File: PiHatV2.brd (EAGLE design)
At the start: 65.8 x 56.4 mm, 29 parts, among them U1 RASPBERRY_PI_3_MODEL_B+, X2 SCREENBREAKOUT_SCREENBREAKOUT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

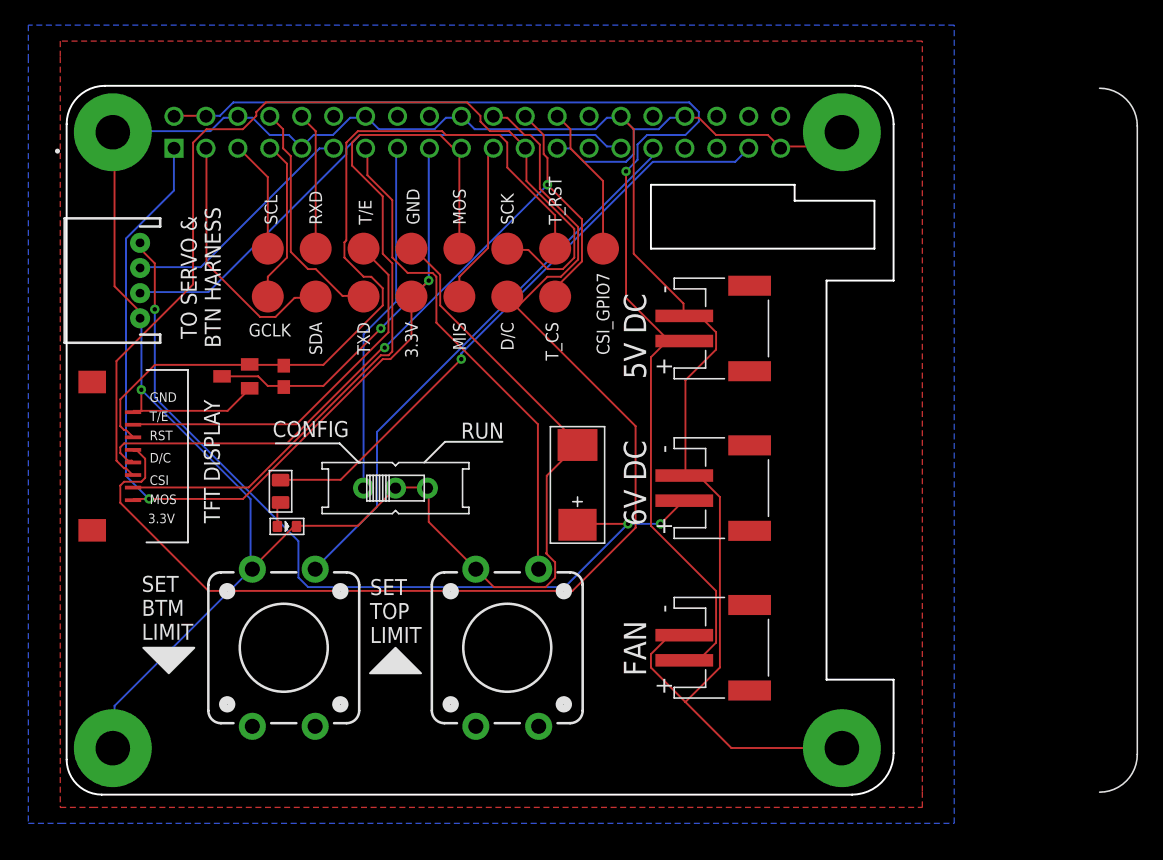
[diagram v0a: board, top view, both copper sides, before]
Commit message: support for a limit switch button for cont servo
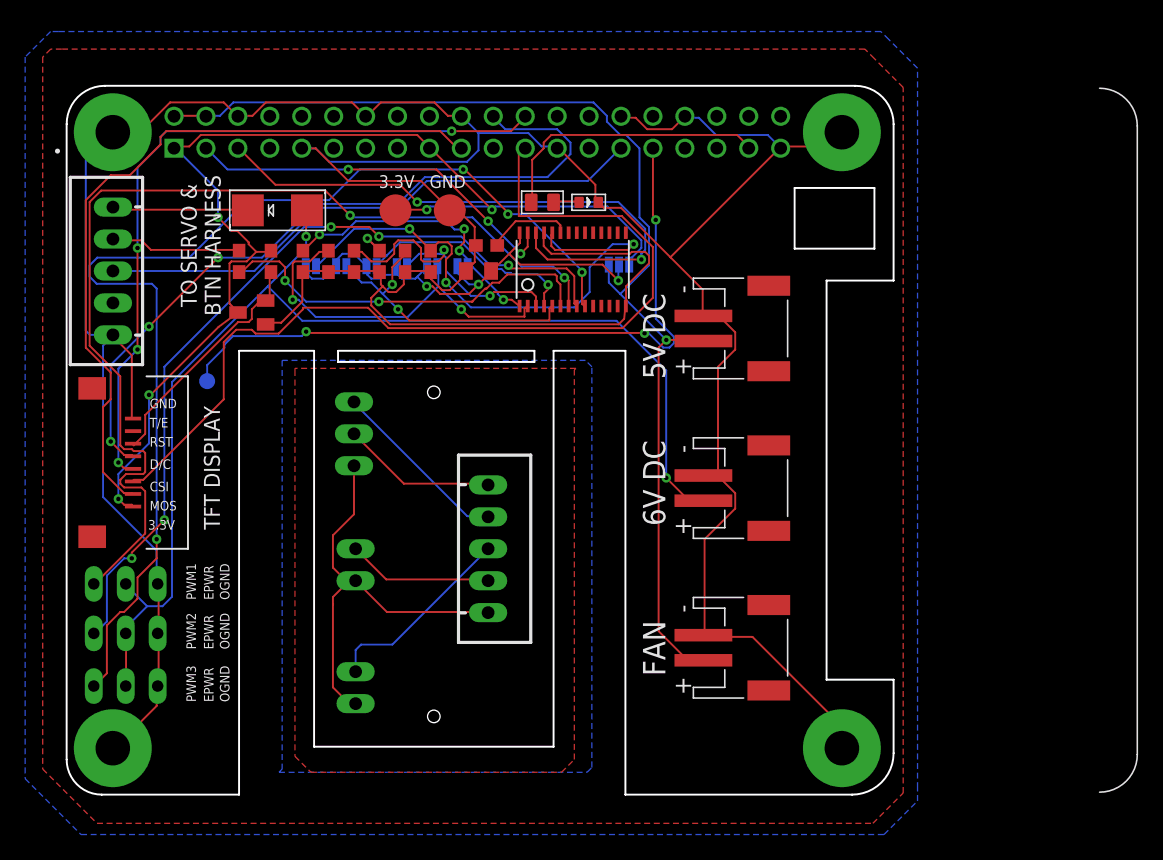
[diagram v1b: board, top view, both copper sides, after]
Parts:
- removed C1: 470uf, Seeed-Capacitor:AVX-D
- removed S1: (no value), adafruit:EG1218
- removed S2, S3: SPARKFUN-SWITCHES_MOMENTARY-SWITCH-SPST-PTH-12MM, ARDUINO_3V_TTL_INTERFACE_2_PI:SPARKFUN-SWITCHES_TACTILE_SWITCH_PTH_12MM
- removed SERVO_BTN_HARNESS: (no value), SparkFun-Connectors:JST-4-PTH
- removed TP1, TP10, TP11, TP12, TP13, TP14, TP15, TP2, TP3, TP4, TP5, TP6, TP9: TPB2,54, testpad:B2,54
- added C2: 10uF, adafruit:C0805K
- added D1: (no value), adafruit:SMADIODE
- added IO_LEVEL: JUMPER-SMT_3_NO_NO-SILK, SparkFun-Jumpers:SMT-JUMPER_3_NO_NO-SILK
- added JP1, JP2, JP3: (no value), FeatherWing:LED-BADGE_SCHEMATIC_JUMPER_JP2
- added JP4, JP5, JP6, JP7, JP8, JP9: JUMPER-SMT_2_NO_NO-SILK, SparkFun-Jumpers:SMT-JUMPER_2_NO_NO-SILK
- added LIM_BTN: TESTPAD_TPSQB1,27, ARDUINO_3V_TTL_INTERFACE_2_PI:TESTPAD_B1,27
- added R10, R2, R5, R6, R7, R8, R9: 10k, PiHat:ARDUINO_3V_TTL_INTERFACE_2_PI_SPARKFUN-RESISTORS_0603:1
- added R4: 220, PiHat:ARDUINO_3V_TTL_INTERFACE_2_PI_SPARKFUN-RESISTORS_0603:1
- added U2: (no value), adafruit:TSSOP28
- added X1, X3: JST-XH-05-PIN-LONG-PAD, Rembrandt Electronics - JST XH Connectors v1-0:JST-XH-05-PACKAGE-LONG-PAD
- added X4: JST-XH-03-PIN-LONG-PAD, Rembrandt Electronics - JST XH Connectors v1-0:JST-XH-03-PACKAGE-LONG-PAD
- added X5, X6: JST-XH-02-PIN-LONG-PAD, Rembrandt Electronics - JST XH Connectors v1-0:JST-XH-02-PACKAGE-LONG-PAD
- moved D2 35.2 mm to (44.6, 25.3)
- moved R3 31.0 mm to (40.9, 25.3), turned to 90 degrees
- moved R1 9.20 mm to (19.3, 20.6), turned to 270 degrees
- moved TP7 6.97 mm to (29.2, 24.6)
- moved APX803 5.24 mm to (17.8, 16.5)
- moved TP8 4.31 mm to (33.5, 24.6)
- moved 5V_IO 1.52 mm to (57.4, 15.2)
- moved FAN 1.52 mm to (57.4, -10.2)
- moved SERVO_PWR 1.52 mm to (57.4, 2.54)
- moved X2 0.51 mm to (5.08, 4.57)
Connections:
- removed net CONFIG: S1.O, U1.15
- removed net DOWN: S3.1, U1.31
- removed net GPCLK0: TP6.TP, U1.7
- removed net RX: TP3.TP, U1.10
- removed net TX: TP2.TP, U1.8
- removed net UP: S2.1, U1.13
- new net A0: JP4.1, R5.2, U2.1
- new net A1: JP5.1, R6.2, U2.2
- new net A2: JP6.1, R7.2, U2.3
- new net A3: JP7.1, R8.2, U2.4
- new net A4: JP8.1, R9.2, U2.5
- new net A5: JP9.1, R10.2, U2.24
- new net BB_BTN: X3.3, X6.2
- new net BB_GND: X3.5, X4.1, X5.1, X6.1
- new net BB_LIM_BTN: X3.4, X5.2
- new net BB_SERVO: X3.2, X4.3
- new net BB_SER_PWR: X3.1, X4.2
- new net LIM_BTN: LIM_BTN.TP, U1.31, X1.2
- new net N$5: R4.1, U2.6
- new net N$6: D1.C, X1.5
- new net OE: R2.2, U2.23
- new net PWM1: JP1.3, U2.7
- new net PWM2: JP2.3, U2.8
- new net PWM3: JP3.3, U2.9
- new net VDDIO: C2.1, IO_LEVEL.2, JP4.2, JP5.2, JP6.2, JP7.2, JP8.2, JP9.2, U2.28
- net 3.3V: now also IO_LEVEL.3
- net 5V: now also IO_LEVEL.1
- net BTN: now also X1.3; no longer SERVO_BTN_HARNESS.2
- net CS1: no longer TP15.TP
- net D/C: no longer TP12.TP
- net GND: now also C2.2, JP1.1, JP2.1, JP3.1, R10.1, R2.1, R5.1, R6.1, R7.1, R8.1, R9.1, U2.14, U2.25, X1.1; no longer C1.-, S1.P, S1.S, S2.3, S3.3, SERVO_BTN_HARNESS.1
- net MISO: no longer TP10.TP
- net MOSI: no longer TP9.TP
- net SCK: no longer TP11.TP
- net SCL: now also U2.26; no longer TP5.TP
- net SDA: now also U2.27; no longer TP4.TP
- net SERVO: now also R4.2, X1.4; no longer SERVO_BTN_HARNESS.3, U1.11
- net SER_PWR: now also D1.A, JP1.2, JP2.2, JP3.2; no longer C1.+, SERVO_BTN_HARNESS.4
- net TE: no longer TP1.TP
- net TFT_!RST: no longer TP13.TP
- net TFT_CS: no longer TP14.TP
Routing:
- net PWM3: track 0.00 -> 89.2 mm, vias 0 -> 4
- net PWM1: track 0.00 -> 81.6 mm, vias 0 -> 2
- net PWM2: track 0.00 -> 65.2 mm, vias 0 -> 5
- net LIM_BTN: track 0.00 -> 56.5 mm, vias 0 -> 3
- net TFT_!RST: track 65.8 -> 20.2 mm
- net DOWN: track 44.6 -> 0.00 mm
- net A5: track 0.00 -> 43.2 mm, vias 0 -> 3
- net UP: track 40.4 -> 0.00 mm
- net VDDIO: track 0.00 -> 38.9 mm, vias 0 -> 3
- net SCL: track 9.02 -> 47.6 mm, vias 0 -> 2
- net D/C: track 97.7 -> 59.8 mm, vias 0 -> 3
- net BB_GND: track 0.00 -> 34.6 mm
- net N$5: track 0.00 -> 31.2 mm, vias 0 -> 2
- net TE: track 30.8 -> 0.07 mm
- net A1: track 0.00 -> 29.8 mm, vias 0 -> 2
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- added copper zone on layer 1, net BB_GND
- added copper zone on layer 16, net BB_SER_PWR
- added copper zone on layer 16, net SER_PWR
- removed copper zone on layer 16, net GND
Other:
- outline, holes or cut-outs redrawn
- board text added: "5.0V"
- board text added: "A0"
- board text added: "A1"
- board text added: "A2"
- board text added: "A3"
- board text added: "A4"
- board text added: "A5"
- board text added: "EPWR"
- board text added: "I2C ADDRESS SELECTORS"
- board text added: "LOGIC LEVEL SELECTOR"
- board text added: "OGND"
- board text added: "PWM1"
- board text added: "PWM2"
- board text added: "PWM3"
- board text added: "[OPEN=0 | CLOSED=1]"
- board text removed: "CONFIG"
- board text removed: "CSI_GPIO7"
- board text removed: "GCLK"
- board text removed: "MIS"
- board text removed: "RUN"
- board text removed: "RXD"
- board text removed: "SCK"
- board text removed: "SCL"
- board text removed: "SDA"
- board text removed: "SET BTM LIMIT"
- board text removed: "SET TOP LIMIT"
- board text removed: "TXD"
- board text removed: "T_CS"
- board text removed: "T_RST"
